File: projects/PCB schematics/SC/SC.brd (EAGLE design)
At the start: 135.9 x 86 mm, 75 parts, among them X1 5566-10, X2 5566-2, X4 5566-12

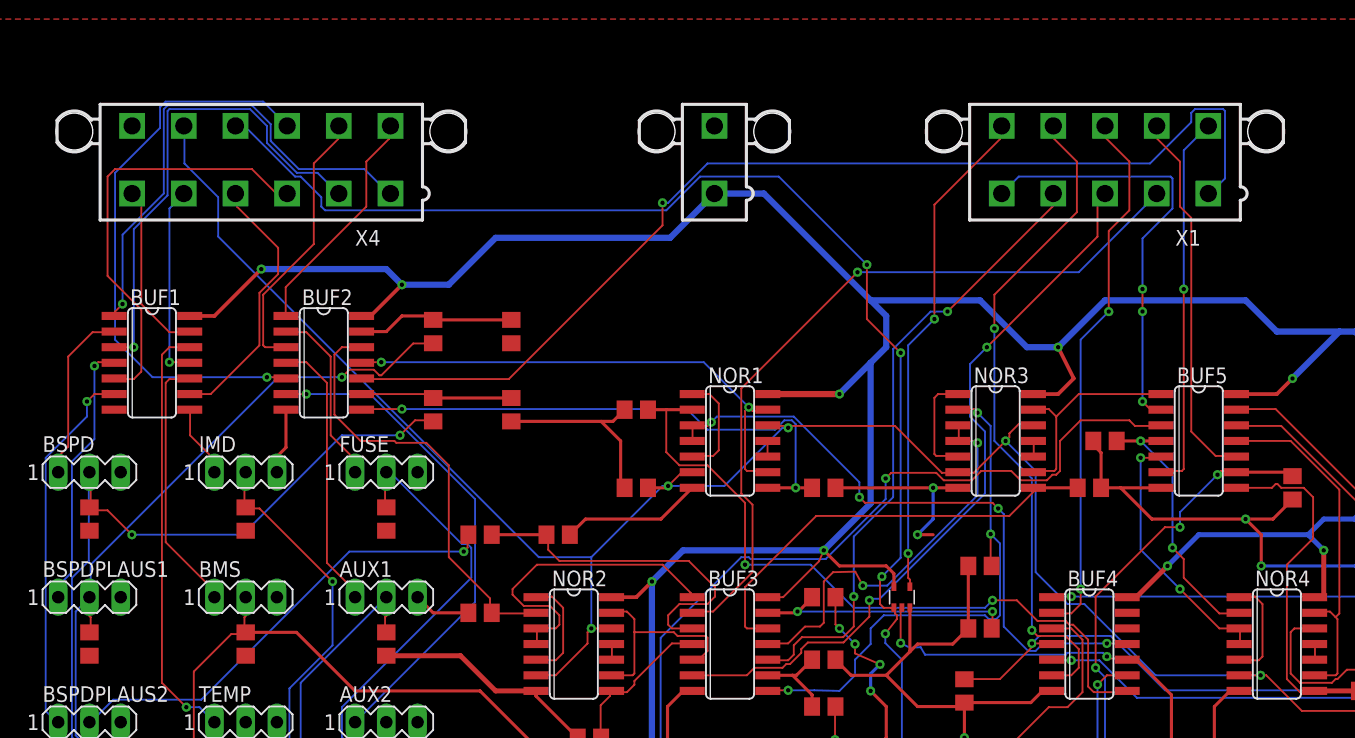
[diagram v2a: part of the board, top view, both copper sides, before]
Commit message: SC - Silkscreen tidy.
Many silkscreen labels were previously unreadable.
This commit consisted of moving labels into readable positions
without as much via obstruction.
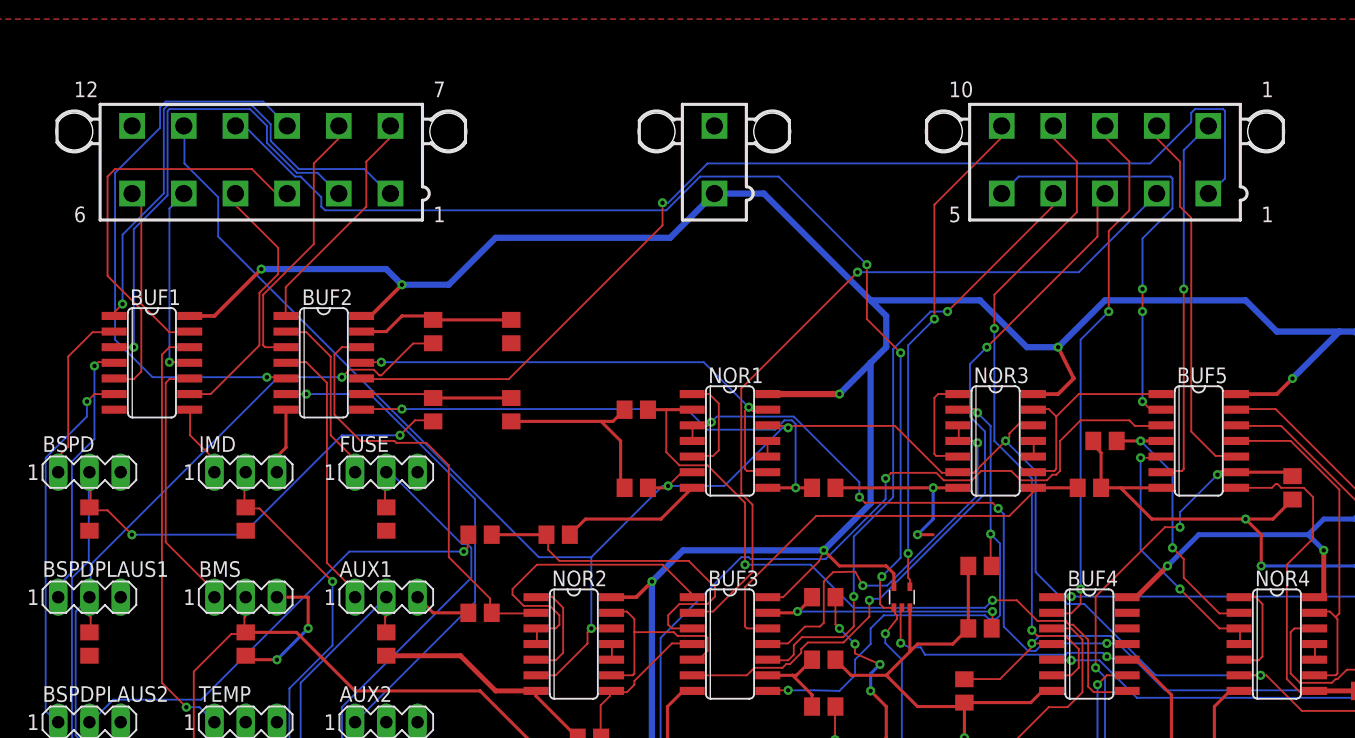
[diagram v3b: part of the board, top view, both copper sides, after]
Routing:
- net GND: track 306.7 -> 318.0 mm, vias 7 -> 9
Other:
- board text added: "1"
- board text added: "10"
- board text added: "12"
- board text added: "5"
- board text added: "6"
- board text added: "7"

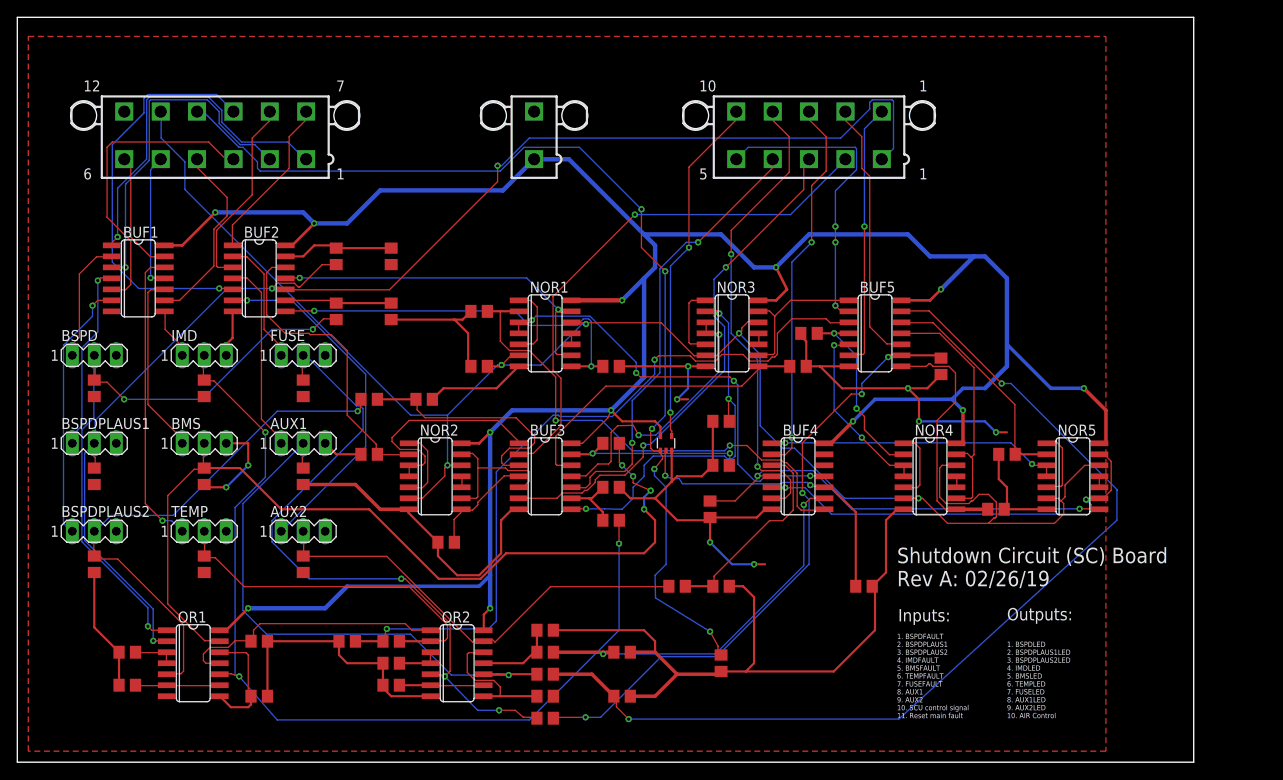
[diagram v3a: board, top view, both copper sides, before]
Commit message: SC - Rev B; Board size reduction.
Board size was able to be further minimized.
Components moved closed together and board footprint reduced.
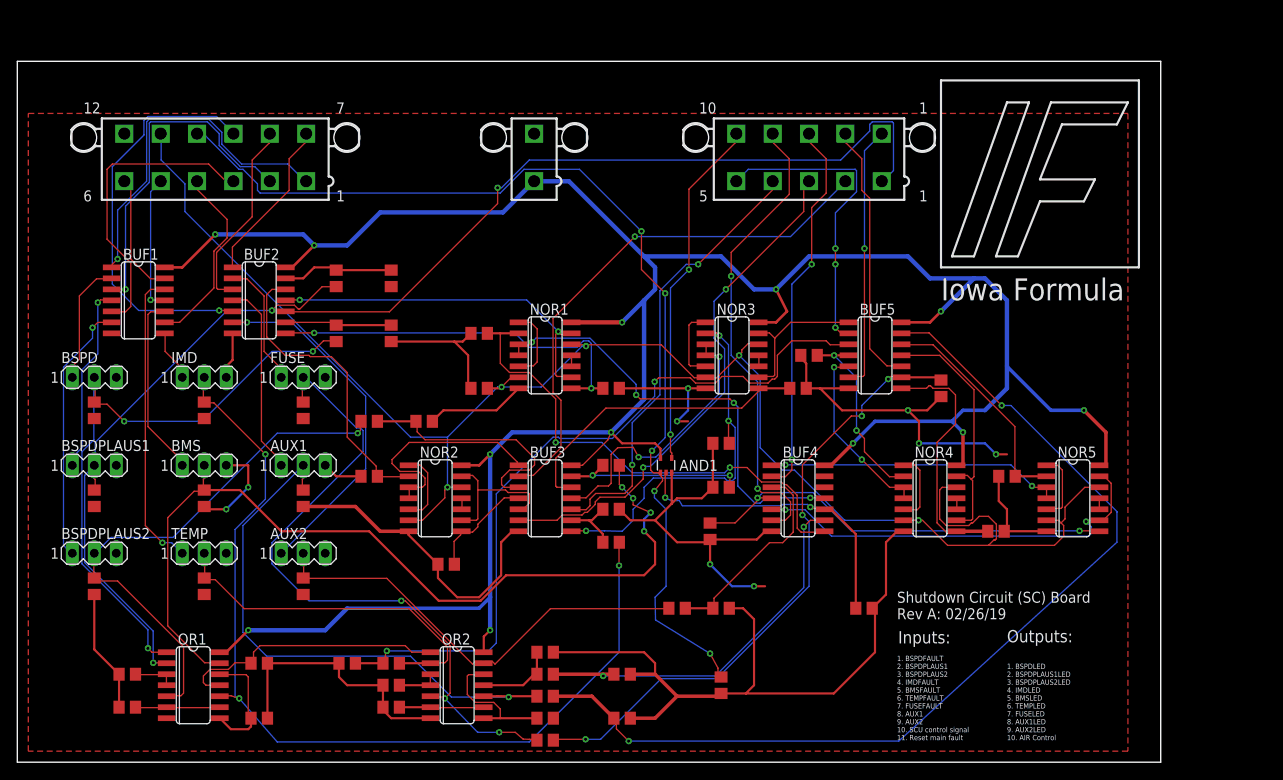
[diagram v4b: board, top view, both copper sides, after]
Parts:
- moved X1 2.54 mm to (91.4, 69.8)
- moved X2 2.54 mm to (59.7, 69.8)
- moved X4 2.54 mm to (22.9, 69.8)
- moved AUX2 2.54 mm to (33.0, 24.1)
- moved BSPDPLAUS2 2.54 mm to (8.89, 24.1)
- moved BUF3 2.54 mm to (61.0, 30.5)
- moved BUF4 2.54 mm to (90.2, 30.5)
- moved NOR2 2.54 mm to (48.3, 30.5)
- moved NOR4 2.54 mm to (105.4, 30.5)
- moved NOR5 2.54 mm to (121.9, 30.5)
- moved R1 2.54 mm to (8.89, 30.5)
- moved R32 2.54 mm to (68.6, 25.4)
- moved R5 2.54 mm to (21.6, 30.5)
- moved R8 2.54 mm to (33.0, 30.5)
- moved TEMP 2.54 mm to (21.6, 24.1)
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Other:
- board size 135.9 x 86 mm -> 132.1 x 81 mm
